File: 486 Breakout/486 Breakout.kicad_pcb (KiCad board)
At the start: 4 copper layers, 100 x 100 mm, 50 parts, among them J1 PWR, J10 Conn_02x03_Counter_Clockwise, J11 Byte Enabled, J12 FPU, J13 Input, J14 Bus Size, J15 Bus Arbitration, J2 Conn_02x04_Counter_Clockwise, J3 Not Connected, J4 Address Bus, J5 Data Bus, J6 Conn_02x03_Counter_Clockwise, J7 Control Bus, J8 Cache, J9 Parity, U1 80486DX, U2 7400, U3 7400

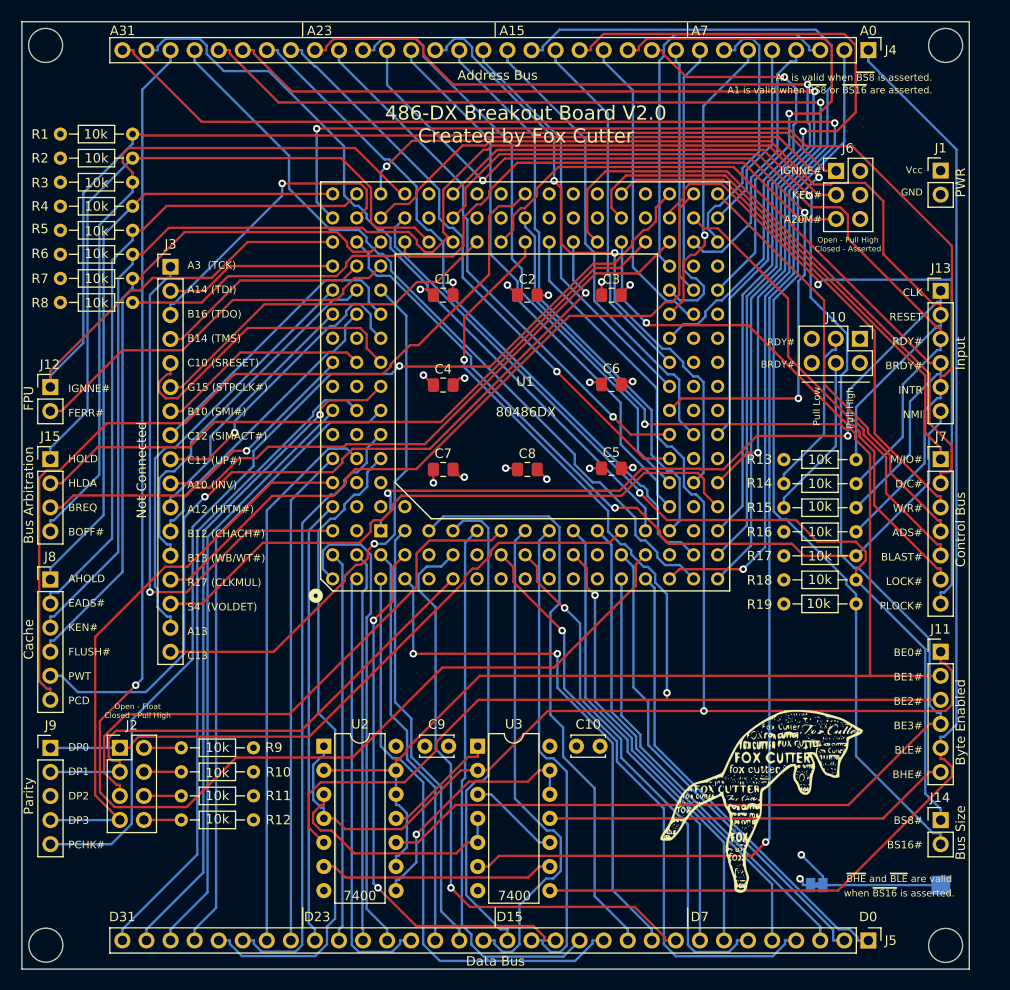
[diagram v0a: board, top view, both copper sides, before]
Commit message: * Updating  the 486 PCB * TestRom2 added
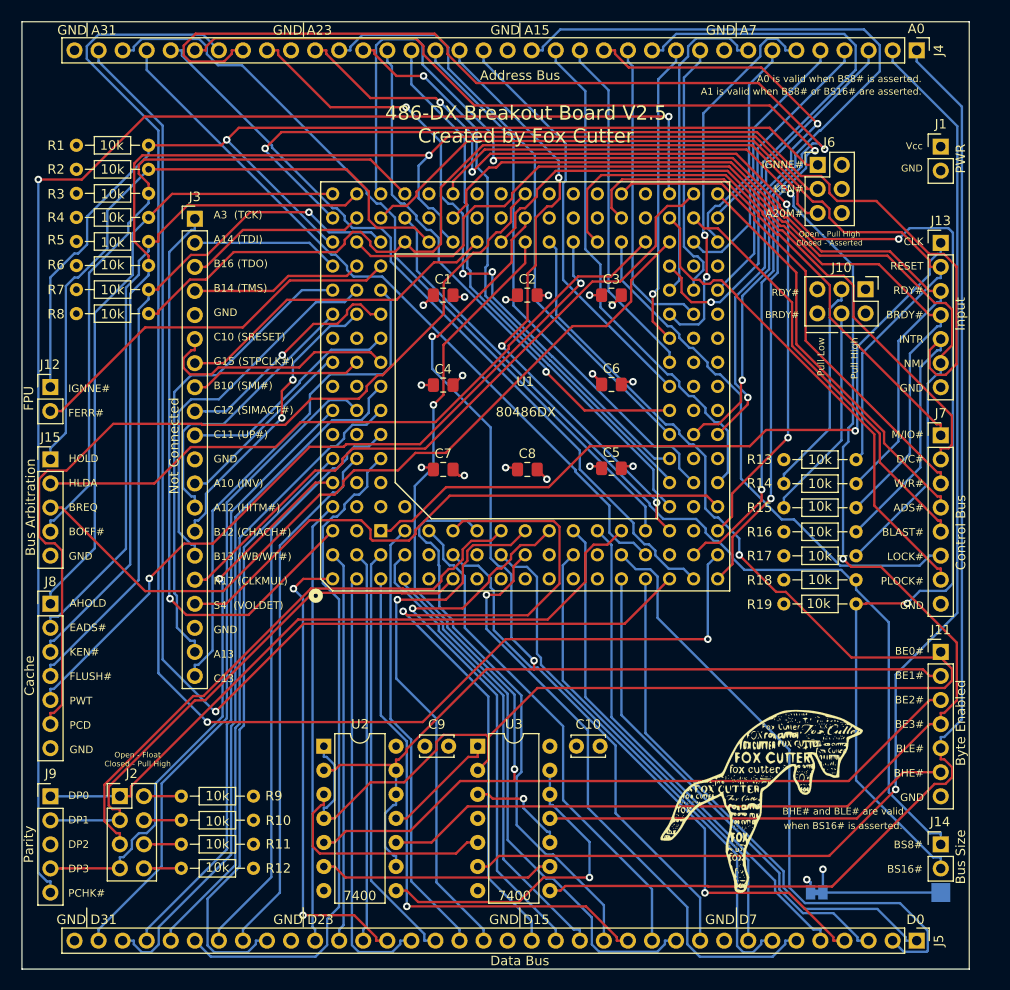
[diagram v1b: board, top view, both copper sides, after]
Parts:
- J11, J13, J8: footprint Connector_PinHeader_2.54mm:PinHeader_1x06_P2.54mm_Vertical -> Connector_PinHeader_2.54mm:PinHeader_1x07_P2.54mm_Vertical
- J15: footprint Connector_PinHeader_2.54mm:PinHeader_1x04_P2.54mm_Vertical -> Connector_PinHeader_2.54mm:PinHeader_1x05_P2.54mm_Vertical
- J3: footprint Connector_PinHeader_2.54mm:PinHeader_1x17_P2.54mm_Vertical -> Connector_PinHeader_2.54mm:PinHeader_1x20_P2.54mm_Vertical
- J4, J5: footprint Connector_PinHeader_2.54mm:PinHeader_1x32_P2.54mm_Vertical -> Connector_PinHeader_2.54mm:PinHeader_1x36_P2.54mm_Vertical
- J7: footprint Connector_PinHeader_2.54mm:PinHeader_1x07_P2.54mm_Vertical -> Connector_PinHeader_2.54mm:PinHeader_1x08_P2.54mm_Vertical
- moved J3 5.68 mm to (88.2, 70.8)
- moved J10 5.26 mm to (159.1, 78.2)
- moved R12 5.11 mm to (86.8, 139.4)
- moved J2 5.11 mm to (80.3, 131.7)
- moved R9 5.11 mm to (86.8, 131.7)
- moved J9 5.10 mm to (73.0, 131.8)
- moved R10 5.10 mm to (86.8, 134.3)
- moved R11 5.10 mm to (86.8, 136.8)
- moved J4 5.10 mm to (164.4, 53.0)
- moved J5 5.10 mm to (164.4, 147.0)
- moved J13 5.06 mm to (167.0, 73.3)
- moved J14 2.56 mm to (167.0, 136.8)
- moved J8 2.56 mm to (73.0, 111.4)
- moved J1 2.53 mm to (167.0, 63.2)
- moved J7 2.52 mm to (167.0, 93.7)
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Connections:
- J3 pad 10: NC_A10 -> NC_C11
- J3 pad 11: NC_A12 -> GND
- J3 pad 12: NC_B12 -> NC_A10
- J3 pad 13: NC_B13 -> NC_A12
- J3 pad 14: NC_R17 -> NC_B12
- J3 pad 15: NC_S4 -> NC_B13
- J3 pad 16: NC_A13 -> NC_R17
- J3 pad 17: NC_C13 -> NC_S4
- J3 pad 5: NC_C10 -> GND
- J3 pad 6: NC_G15 -> NC_C10
- J3 pad 7: NC_B10 -> NC_G15
- J3 pad 8: NC_C12 -> NC_B10
- J3 pad 9: NC_C11 -> NC_C12
- J4 pad 10: A9 -> A8
- J4 pad 11: A10 -> A9
- J4 pad 12: A11 -> A10
- J4 pad 13: A12 -> A11
- J4 pad 14: A13 -> A12
- J4 pad 15: A14 -> A13
- J4 pad 16: A15 -> A14
- J4 pad 17: A16 -> A15
- J4 pad 18: A17 -> GND
- J4 pad 19: A18 -> A16
- J4 pad 20: A19 -> A17
- J4 pad 21: A20 -> A18
- J4 pad 22: A21 -> A19
- J4 pad 23: A22 -> A20
- J4 pad 24: A23 -> A21
- J4 pad 25: A24 -> A22
- J4 pad 26: A25 -> A23
- J4 pad 27: A26 -> GND
- J4 pad 28: A27 -> A24
- J4 pad 29: A28 -> A25
- J4 pad 30: A29 -> A26
- J4 pad 31: A30 -> A27
- J4 pad 32: A31 -> A28
- J4 pad 9: A8 -> GND
- J5 pad 10: D9 -> D8
- J5 pad 11: D10 -> D9
- J5 pad 12: D11 -> D10
- J5 pad 13: D12 -> D11
- J5 pad 14: D13 -> D12
- J5 pad 15: D14 -> D13
- J5 pad 16: D15 -> D14
- J5 pad 17: D16 -> D15
- J5 pad 18: D17 -> GND
- J5 pad 19: D18 -> D16
- J5 pad 20: D19 -> D17
- J5 pad 21: D20 -> D18
- J5 pad 22: D21 -> D19
- J5 pad 23: D22 -> D20
- J5 pad 24: D23 -> D21
- J5 pad 25: D24 -> D22
- J5 pad 26: D25 -> D23
- J5 pad 27: D26 -> GND
- J5 pad 28: D27 -> D24
- J5 pad 29: D28 -> D25
- J5 pad 30: D29 -> D26
- J5 pad 31: D30 -> D27
- J5 pad 32: D31 -> D28
- J5 pad 9: D8 -> GND
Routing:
- net A29: track 152.0 -> 78.0 mm, vias 1 -> 0
- net A25: track 74.2 -> 133.0 mm, vias 0 -> 2
- net PCHK#: track 110.4 -> 153.5 mm, vias 1 -> 2
- net A26: track 115.6 -> 157.5 mm, vias 1 -> 2
- net A15: track 49.1 -> 88.8 mm, vias 0 -> 1
- net BS16#: track 132.4 -> 169.8 mm, vias 2 -> 3
- net A20: track 89.3 -> 56.1 mm, vias 3 -> 1
- net A14: track 85.3 -> 54.4 mm, vias 1 -> 0
- net IGNNE#: track 143.6 -> 118.7 mm, vias 0 -> 1
- net D15: track 51.7 -> 76.4 mm, vias 0 -> 1
- net PLOCK#: track 71.8 -> 52.3 mm, vias 1 -> 0
- net NMI: track 87.1 -> 106.2 mm, vias 1 -> 0
- net BE1#: track 157.3 -> 139.1 mm, vias 1 -> 2
- net A9: track 50.2 -> 32.1 mm
- net A12: track 79.8 -> 64.3 mm, vias 1 -> 2
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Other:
- outline, holes or cut-outs redrawn
- board text added: "486-DX Breakout Board V2.5 Created by Fox Cutter"
- board text added: "A0 is valid when BS8# is asserted."
- board text added: "A1 is valid when BS8# or BS16# are asserted."
- board text added: "A3 (TCK) A14 (TDI) B16 (TDO) B14 (TMS) GND C10 (SRESET) G15 (STPCLK#) B10 (SMI#) C12 (SIMACT#) C11 (UP#) GND A10 (INV) A12 (HITM#) B12 (CHACH#) B13 (WB/WT#) R17 (CLKMUL) S4 (VOLDET) GND A13 C13"
- board text added: "AHOLD EADS# KEN# FLUSH# PWT PCD GND"
- board text added: "BE0# BE1# BE2# BE3# BLE# BHE# GND"
- board text added: "BHE# and BLE# are valid"
- board text added: "CLK RESET RDY# BRDY# INTR NMI GND"
- board text added: "For a 3.3v CPU using 5v logic, break JP1 and connect TP1 to +5v (Double check with Datasheet first)"
- board text added: "GND A15"
- board text added: "GND A23"
- board text added: "GND A31"
- board text added: "GND A7"
- board text added: "GND D15"
- board text added: "GND D23"
- board text added: "GND D31"
- board text added: "GND D7"
- board text added: "HOLD HLDA BREQ BOFF# GND"
- board text added: "M/IO# D/C# W/R# ADS# BLAST# LOCK# PLOCK# GND"
- board text added: "when BS16# is asserted."
- board text removed: "486-DX Breakout Board V2.0 Created by Fox Cutter"
- board text removed: "A0 is valid when ~{BS8} is asserted."
- board text removed: "A1 is valid when ~{BS8} or ~{BS16} are asserted."
- board text removed: "A15"
- board text removed: "A23"
- board text removed: "A3 (TCK) A14 (TDI) B16 (TDO) B14 (TMS) C10 (SRESET) G15 (STPCLK#) B10 (SMI#) C12 (SIMACT#) C11 (UP#) A10 (INV) A12 (HITM#) B12 (CHACH#) B13 (WB/WT#) R17 (CLKMUL) S4 (VOLDET) A13 C13"
- board text removed: "A31"
- board text removed: "A7"
- board text removed: "AHOLD EADS# KEN# FLUSH# PWT PCD"
- board text removed: "BE0# BE1# BE2# BE3# BLE# BHE#"
- board text removed: "CLK RESET RDY# BRDY# INTR NMI"
- board text removed: "D15"
- board text removed: "D23"
- board text removed: "D31"
- board text removed: "D7"
- board text removed: "HOLD HLDA BREQ BOFF#"
- board text removed: "M/IO# D/C# W/R# ADS# BLAST# LOCK# PLOCK#"
- board text removed: "when ~{BS16} is asserted."
- board text removed: "~{BHE} and ~{BLE} are valid"

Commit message: Minor PCB updates, and adding Gerber files
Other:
- board text added: "JLCJLCJLCJLC"
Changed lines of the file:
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@@
     (fp_line (start -1 0.625) (end -1 -0.625) (layer "F.Fab") (width 0.1))
     (fp_line (start -1 -0.625) (end 1 -0.625) (layer "F.Fab") (width 0.1))
-    (pad "1" smd roundrect (at -1.0375 0) (size 1.175 1.45) (layers "F.Cu" "F.Paste" "F.Mask") (roundrect_rratio 0.212766)
+    (pad "1" smd roundrect (at -1.0375 0) (size 1.175 1.45) (layers "F.Cu" "F.Paste" "F.Mask") (roundrect_rratio 0.2127659574)
       (net 1 "GND") (pintype "passive"))
-    (pad "2" smd roundrect (at 1.0375 0) (size 1.175 1.45) (layers "F.Cu" "F.Paste" "F.Mask") (roundrect_rratio 0.212766)
+    (pad "2" smd roundrect (at 1.0375 0) (size 1.175 1.45) (layers "F.Cu" "F.Paste" "F.Mask") (roundrect_rratio 0.2127659574)
       (net 134 "VCC") (pintype "passive"))
     (model "${KICAD6_3DMODEL_DIR}/Capacitor_SMD.3dshapes/C_0805_2012Metric.wrl"
@@
     (fp_line (start 1 -0.625) (end 1 0.625) (layer "F.Fab") (width 0.1))
     (fp_line (start -1 -0.625) (end 1 -0.625) (layer "F.Fab") (width 0.1))
-    (pad "1" smd roundrect (at -1.0375 0) (size 1.175 1.45) (layers "F.Cu" "F.Paste" "F.Mask") (roundrect_rratio 0.212766)
+    (pad "1" smd roundrect (at -1.0375 0) (size 1.175 1.45) (layers "F.Cu" "F.Paste" "F.Mask") (roundrect_rratio 0.2127659574)
       (net 1 "GND") (pintype "passive"))
-    (pad "2" smd roundrect (at 1.0375 0) (size 1.175 1.45) (layers "F.Cu" "F.Paste" "F.Mask") (roundrect_rratio 0.212766)
+    (pad "2" smd roundrect (at 1.0375 0) (size 1.175 1.45) (layers "F.Cu" "F.Paste" "F.Mask") (roundrect_rratio 0.2127659574)
       (net 134 "VCC") (pintype "passive"))
     (model "${KICAD6_3DMODEL_DIR}/Capacitor_SMD.3dshapes/C_0805_2012Metric.wrl"
@@
     (fp_line (start 1 0.625) (end -1 0.625) (layer "F.Fab") (width 0.1))
     (fp_line (start -1 -0.625) (end 1 -0.625) (layer "F.Fab") (width 0.1))
-    (pad "1" smd roundrect (at -1.0375 0) (size 1.175 1.45) (layers "F.Cu" "F.Paste" "F.Mask") (roundrect_rratio 0.212766)
+    (pad "1" smd roundrect (at -1.0375 0) (size 1.175 1.45) (layers "F.Cu" "F.Paste" "F.Mask") (roundrect_rratio 0.2127659574)
       (net 1 "GND") (pintype "passive"))
-    (pad "2" smd roundrect (at 1.0375 0) (size 1.175 1.45) (layers "F.Cu" "F.Paste" "F.Mask") (roundrect_rratio 0.212766)
+    (pad "2" smd roundrect (at 1.0375 0) (size 1.175 1.45) (layers "F.Cu" "F.Paste" "F.Mask") (roundrect_rratio 0.2127659574)
       (net 134 "VCC") (pintype "passive"))
     (model "${KICAD6_3DMODEL_DIR}/Capacitor_SMD.3dshapes/C_0805_2012Metric.wrl"
@@
     (fp_line (start 1 0.625) (end -1 0.625) (layer "F.Fab") (width 0.1))
     (fp_line (start -1 -0.625) (end 1 -0.625) (layer "F.Fab") (width 0.1))
-    (pad "1" smd roundrect (at -1.0375 0) (size 1.175 1.45) (layers "F.Cu" "F.Paste" "F.Mask") (roundrect_rratio 0.212766)
+    (pad "1" smd roundrect (at -1.0375 0) (size 1.175 1.45) (layers "F.Cu" "F.Paste" "F.Mask") (roundrect_rratio 0.2127659574)
       (net 1 "GND") (pintype "passive"))
-    (pad "2" smd roundrect (at 1.0375 0) (size 1.175 1.45) (layers "F.Cu" "F.Paste" "F.Mask") (roundrect_rratio 0.212766)
+    (pad "2" smd roundrect (at 1.0375 0) (size 1.175 1.45) (layers "F.Cu" "F.Paste" "F.Mask") (roundrect_rratio 0.2127659574)
       (net 134 "VCC") (pintype "passive"))
     (model "${KICAD6_3DMODEL_DIR}/Capacitor_SMD.3dshapes/C_0805_2012Metric.wrl"
@@
     (fp_line (start -1 0.625) (end -1 -0.625) (layer "F.Fab") (width 0.1))
     (fp_line (start 1 0.625) (end -1 0.625) (layer "F.Fab") (width 0.1))
-    (pad "1" smd roundrect (at -1.0375 0) (size 1.175 1.45) (layers "F.Cu" "F.Paste" "F.Mask") (roundrect_rratio 0.212766)
+    (pad "1" smd roundrect (at -1.0375 0) (size 1.175 1.45) (layers "F.Cu" "F.Paste" "F.Mask") (roundrect_rratio 0.2127659574)
       (net 1 "GND") (pintype "passive"))
-    (pad "2" smd roundrect (at 1.0375 0) (size 1.175 1.45) (layers "F.Cu" "F.Paste" "F.Mask") (roundrect_rratio 0.212766)
+    (pad "2" smd roundrect (at 1.0375 0) (size 1.175 1.45) (layers "F.Cu" "F.Paste" "F.Mask") (roundrect_rratio 0.2127659574)
       (net 134 "VCC") (pintype "passive"))
     (model "${KICAD6_3DMODEL_DIR}/Capacitor_SMD.3dshapes/C_0805_2012Metric.wrl"
@@
     (fp_line (start 1 0.625) (end -1 0.625) (layer "F.Fab") (width 0.1))
     (fp_line (start -1 -0.625) (end 1 -0.625) (layer "F.Fab") (width 0.1))
-    (pad "1" smd roundrect (at -1.0375 0) (size 1.175 1.45) (layers "F.Cu" "F.Paste" "F.Mask") (roundrect_rratio 0.212766)
+    (pad "1" smd roundrect (at -1.0375 0) (size 1.175 1.45) (layers "F.Cu" "F.Paste" "F.Mask") (roundrect_rratio 0.2127659574)
       (net 1 "GND") (pintype "passive"))
-    (pad "2" smd roundrect (at 1.0375 0) (size 1.175 1.45) (layers "F.Cu" "F.Paste" "F.Mask") (roundrect_rratio 0.212766)
+    (pad "2" smd roundrect (at 1.0375 0) (size 1.175 1.45) (layers "F.Cu" "F.Paste" "F.Mask") (roundrect_rratio 0.2127659574)
       (net 134 "VCC") (pintype "passive"))
     (model "${KICAD6_3DMODEL_DIR}/Capacitor_SMD.3dshapes/C_0805_2012Metric.wrl"
@@
     (fp_line (start -1 0.625) (end -1 -0.625) (layer "F.Fab") (width 0.1))
     (fp_line (start 1 0.625) (end -1 0.625) (layer "F.Fab") (width 0.1))
-    (pad "1" smd roundrect (at -1.0375 0) (size 1.175 1.45) (layers "F.Cu" "F.Paste" "F.Mask") (roundrect_rratio 0.212766)
+    (pad "1" smd roundrect (at -1.0375 0) (size 1.175 1.45) (layers "F.Cu" "F.Paste" "F.Mask") (roundrect_rratio 0.2127659574)
       (net 1 "GND") (pintype "passive"))
-    (pad "2" smd roundrect (at 1.0375 0) (size 1.175 1.45) (layers "F.Cu" "F.Paste" "F.Mask") (roundrect_rratio 0.212766)
+    (pad "2" smd roundrect (at 1.0375 0) (size 1.175 1.45) (layers "F.Cu" "F.Paste" "F.Mask") (roundrect_rratio 0.2127659574)
       (net 134 "VCC") (pintype "passive"))
     (model "${KICAD6_3DMODEL_DIR}/Capacitor_SMD.3dshapes/C_0805_2012Metric.wrl"
@@
     (fp_line (start -1 -0.625) (end 1 -0.625) (layer "F.Fab") (width 0.1))
     (fp_line (start -1 0.625) (end -1 -0.625) (layer "F.Fab") (width 0.1))
-    (pad "1" smd roundrect (at -1.0375 0) (size 1.175 1.45) (layers "F.Cu" "F.Paste" "F.Mask") (roundrect_rratio 0.212766)
+    (pad "1" smd roundrect (at -1.0375 0) (size 1.175 1.45) (layers "F.Cu" "F.Paste" "F.Mask") (roundrect_rratio 0.2127659574)
       (net 1 "GND") (pintype "passive"))
-    (pad "2" smd roundrect (at 1.0375 0) (size 1.175 1.45) (layers "F.Cu" "F.Paste" "F.Mask") (roundrect_rratio 0.212766)
+    (pad "2" smd roundrect (at 1.0375 0) (size 1.175 1.45) (layers "F.Cu" "F.Paste" "F.Mask") (roundrect_rratio 0.2127659574)
       (net 134 "VCC") (pintype "passive"))
     (model "${KICAD6_3DMODEL_DIR}/Capacitor_SMD.3dshapes/C_0805_2012Metric.wrl"
@@
   (footprint "Private_lib:Fox Logo" locked (layer "F.Cu")
     (at 148.16 132.638)
-    (attr through_hole)
+    (attr through_hole board_only)
     (fp_text reference "#LOGO1" (at -0.762 2.032) (layer "F.SilkS") hide
       (effects (font (size 1.524 1.524) (thickness 0.3)))
@@
     (effects (font (size 1 1) (thickness 0.15)))
   )
+  (gr_text "JLCJLCJLCJLC" (at 105.85 134.18 90) (layer "F.SilkS")
+    (effects (font (size 1 1) (thickness 0.15)))
+  )
